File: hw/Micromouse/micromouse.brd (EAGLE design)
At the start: 60 x 97 mm, 47 parts, among them IC1 DSPIC33FJ64MC804-PT, IC2 DRV8833PWR, J1 GP2Y0A51SK0F, J2 GP2Y0A51SK0F, J3 GP2Y0A41SK0F, SW1 B3F-1000

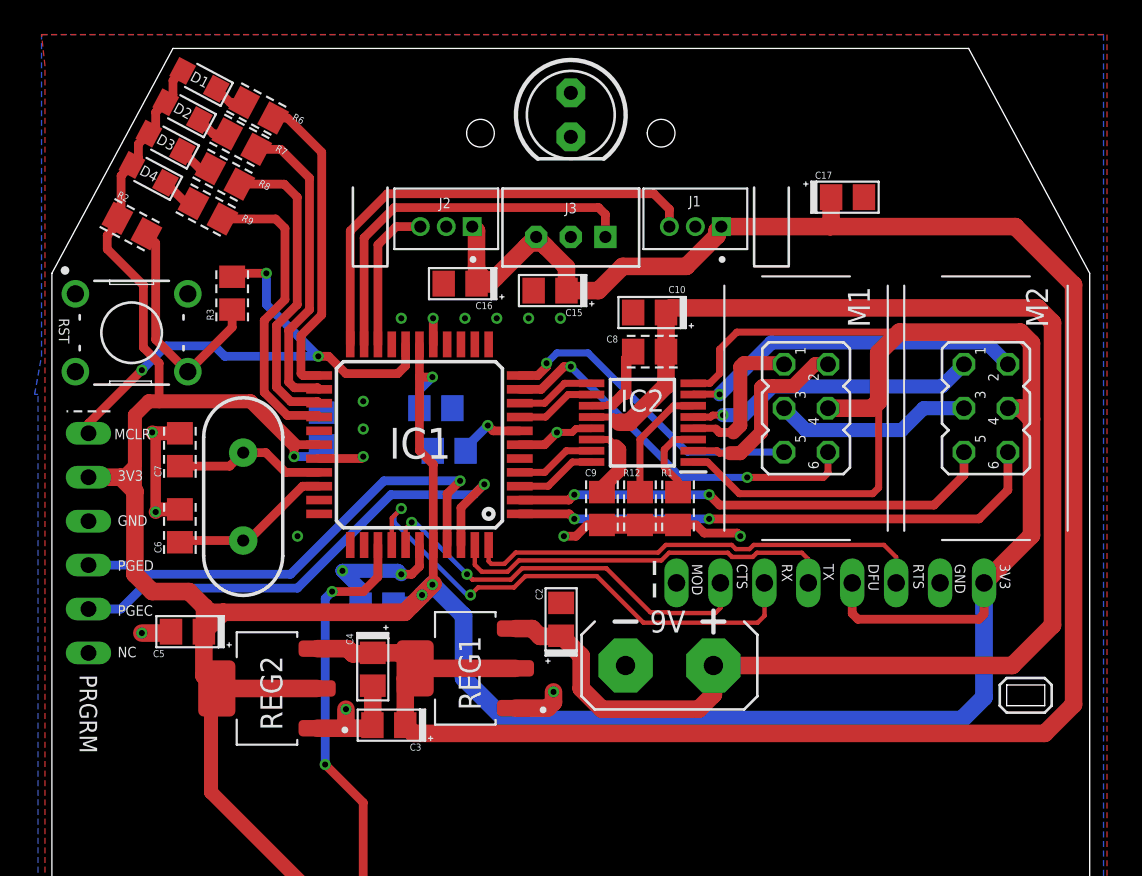
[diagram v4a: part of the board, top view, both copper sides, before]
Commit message: Added silkscreen; Added more space between parts; Added testpoints
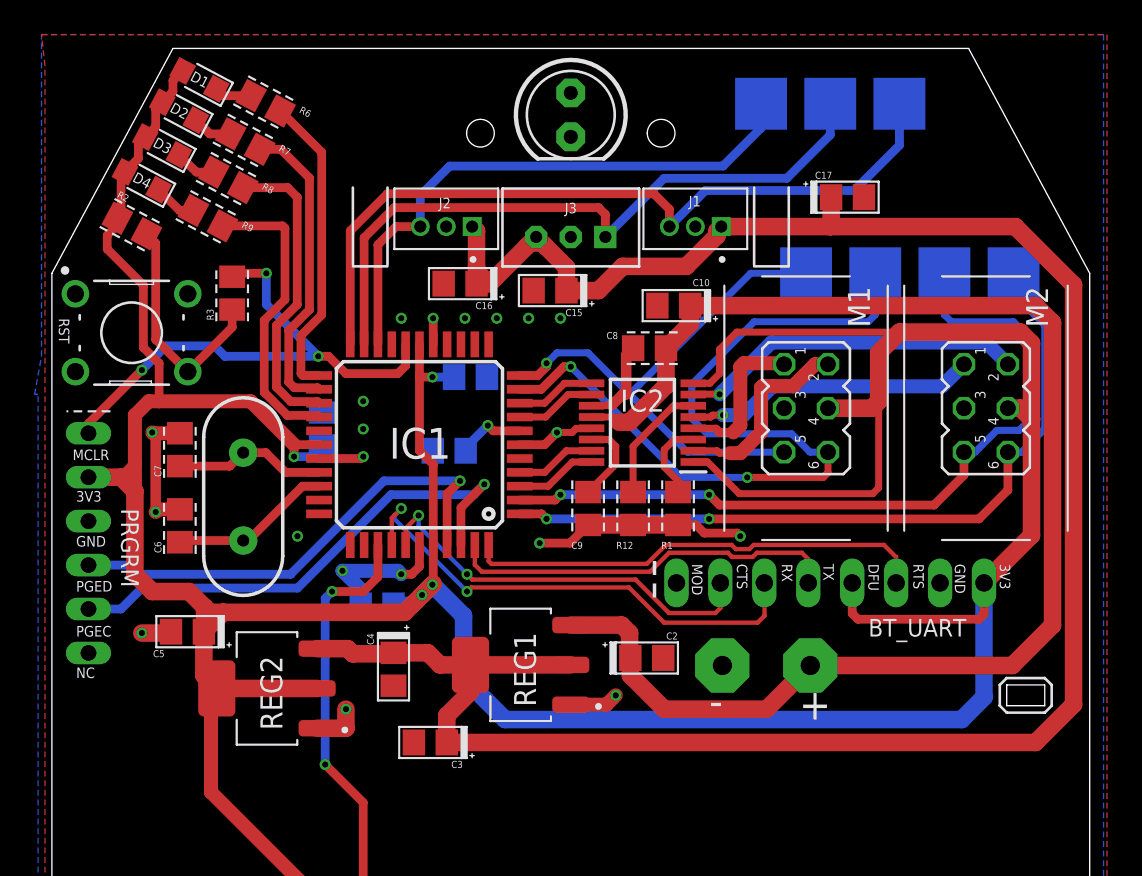
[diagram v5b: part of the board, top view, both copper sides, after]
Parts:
- added P_E1A, P_E1B, P_E2A, P_E2B, P_S1, P_S2, P_S3: (no value), micromouse:PROBEPOINT_SMD
- G1: device battery:AB9V -> micromouse:AB9V
- moved G1 5.60 mm to (11.3, 19.3)
- moved C2 5.44 mm to (4.39, 19.8), turned to 0 degrees
- moved REG1 3.21 mm to (-2.90, 19.4)
- moved C14 2.69 mm to (-5.80, 36.0)
- moved C3 2.60 mm to (-8.12, 14.9)
- moved C10 1.46 mm to (5.96, 40.1)
- moved C4 1.20 mm to (-10.2, 19.1)
- moved C9 0.80 mm to (1.00, 28.4)
- moved R6 0.57 mm to (-17.6, 51.8)
- moved D4 0.57 mm to (-24.8, 47.3)
- moved R9 0.40 mm to (-21.0, 45.2)
- moved R12 0.40 mm to (3.60, 28.4)
- moved D3 0.28 mm to (-23.6, 49.4)
- moved R8 0.28 mm to (-19.8, 47.4)
- moved C8 0.20 mm to (4.55, 37.7)
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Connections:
- net M1_CHA: now also P_E1A.P$1
- net M1_CHB: now also P_E1B.P$1
- net M2_CHA: now also P_E2A.P$1
- net M2_CHB: now also P_E2B.P$1
- net S1_OUT: now also P_S1.P$1
- net S2_OUT: now also P_S2.P$1
- net S3_OUT: now also P_S3.P$1
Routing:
- net M1_CHA: track 22.3 -> 47.6 mm
- net S3_OUT: track 8.64 -> 33.2 mm
- net S1_OUT: track 27.3 -> 44.9 mm
- net M2_CHB: track 28.1 -> 45.4 mm
- net S2_OUT: track 22.3 -> 39.5 mm
- net GND: track 58.3 -> 44.7 mm
- net M1_CHB: track 18.3 -> 31.4 mm
- net M2_CHA: track 31.2 -> 43.7 mm
- net +9V: track 87.0 -> 82.6 mm
- net +5V: track 127.7 -> 130.0 mm
- net +3V3: track 281.6 -> 280.7 mm
- net UART_RX: track 30.1 -> 29.3 mm
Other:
- board text added: "+"
- board text added: "-"
- board text added: "BT_UART"

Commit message: Tweaked schematic and PCB
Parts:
- C11, C13, C14: value (none) -> 100n
- C15, C16, C17: value (none) -> 10u
- P_E1A, P_E1B, P_E2A, P_E2B: device micromouse:PROBEPOINT_SMD -> micromouse:PROBEPOINT_THT
- R1, R12: value 0.2 -> 200m
- R6, R7, R8, R9: value 130 -> 68
- moved P_S1 29.2 mm to (-10.2, 50.2)
- moved P_S2 29.2 mm to (-14.2, 50.2)
- moved P_S3 29.2 mm to (-18.2, 50.2)
- moved P_E1B 12.4 mm to (23.2, 49.8), flipped to the top
- moved P_E1A 11.5 mm to (21.6, 52.8), flipped to the top
- moved P_E2B 5.13 mm to (26.4, 43.8), flipped to the top
- moved P_E2A 4.87 mm to (24.8, 46.8), flipped to the top
- moved C10 1.52 mm to (4.55, 39.5)
- moved C8 0.60 mm to (4.55, 37.1)
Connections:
- net +3V3: no longer IC2.8
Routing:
- net GND: track 44.7 -> 107.4 mm, vias 20 -> 22
- net M1_CHB: track 31.4 -> 45.4 mm
- net +3V3: track 280.7 -> 267.1 mm
- net M1_CHA: track 47.6 -> 58.8 mm
- net S3_OUT: track 33.2 -> 22.3 mm
- net M2_CHA: track 43.7 -> 47.4 mm
- net S2_OUT: track 39.5 -> 43.1 mm
- net +9V: track 82.6 -> 80.7 mm
- net +5V: track 130.0 -> 128.3 mm
- net LED4: track 17.4 -> 15.8 mm
- net LED3: track 17.7 -> 16.1 mm
- net S1_OUT: track 44.9 -> 46.4 mm
- net LED2: track 17.8 -> 16.9 mm
- net N$3: track 5.11 -> 4.39 mm
- net M1-: track 9.02 -> 8.41 mm
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- added copper zone on layer 1, net +3V3
- added copper zone on layer 16, net M1_CHB
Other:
- outline, holes or cut-outs redrawn

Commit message: Added probing points for GND; Small tweaks
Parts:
- added P_GND1, P_GND2, P_GND3: (no value), micromouse:PROBEPOINT_THT
- moved C13 1.34 mm to (-13.8, 34.2)
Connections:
- net GND: now also P_GND1.P$1, P_GND2.P$1, P_GND3.P$1
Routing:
- net GND: track 107.4 -> 44.4 mm, vias 22 -> 21
- net +3V3: track 267.1 -> 260.7 mm
- net +5V: track 128.3 -> 130.8 mm
- net MCLR: track 31.0 -> 31.8 mm
- removed copper zone on layer 1, net +3V3
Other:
- board text added: "RSENSE"

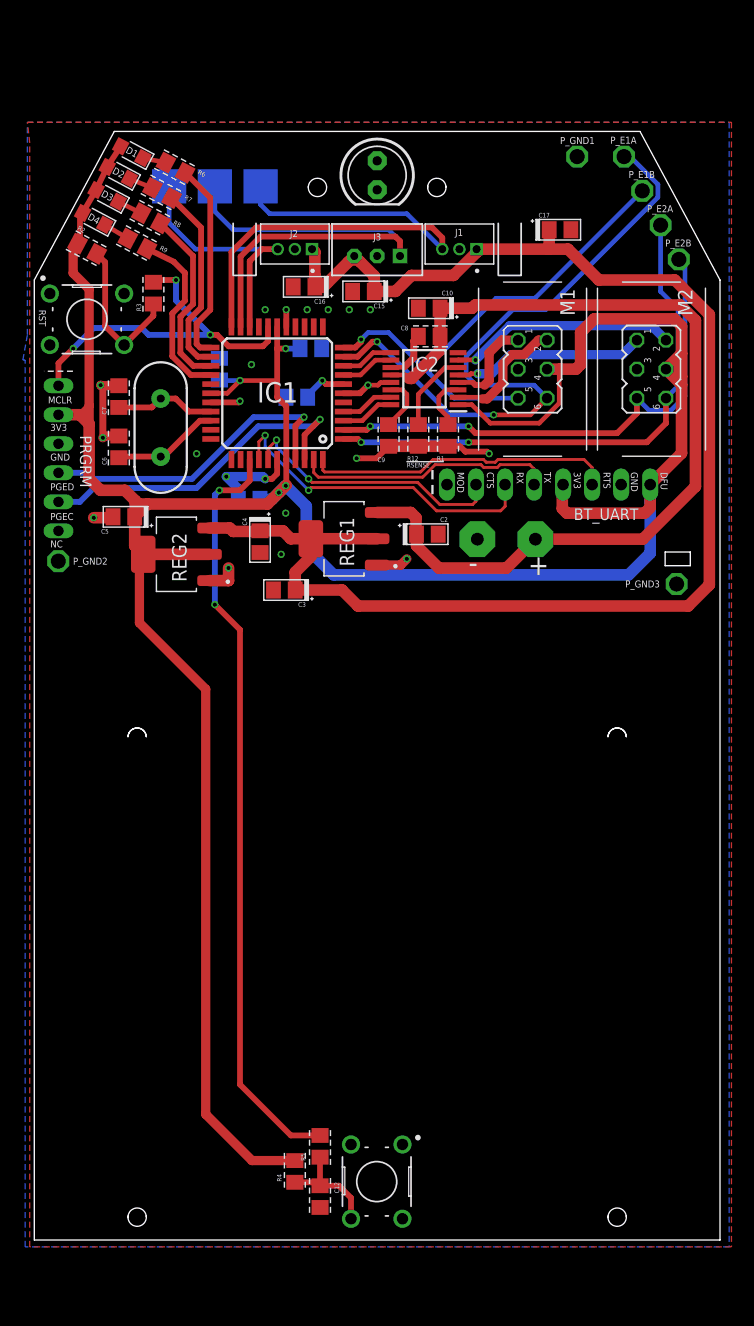
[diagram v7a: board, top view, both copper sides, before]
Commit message: Changes to the board according to design review
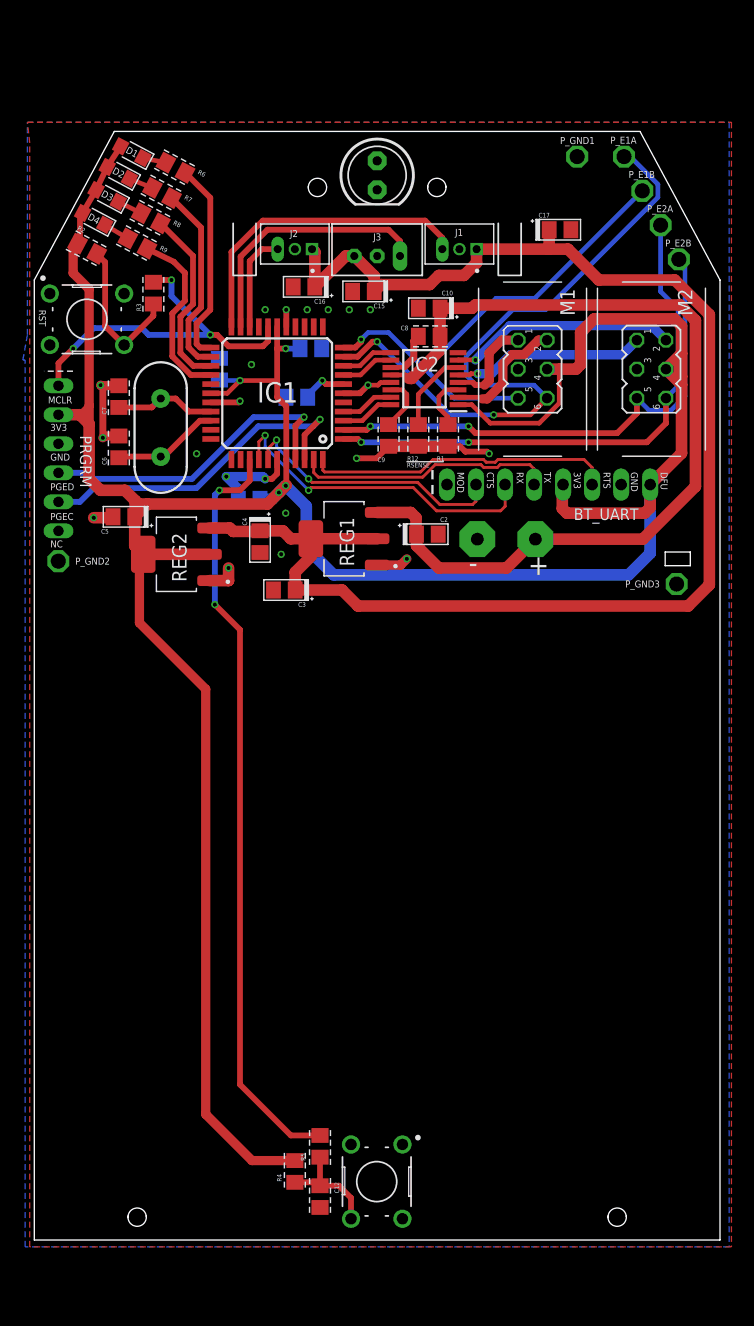
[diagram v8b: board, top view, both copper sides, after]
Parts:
- removed P_S1, P_S2, P_S3: (no value), micromouse:PROBEPOINT_SMD
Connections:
- net S1_OUT: no longer P_S1.P$1
- net S2_OUT: no longer P_S2.P$1
- net S3_OUT: no longer P_S3.P$1
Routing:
- net S2_OUT: track 43.1 -> 22.8 mm
- net S1_OUT: track 46.4 -> 27.8 mm
- net S3_OUT: track 22.3 -> 8.64 mm
- net +5V: track 130.8 -> 128.8 mm
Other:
- outline, holes or cut-outs redrawn
